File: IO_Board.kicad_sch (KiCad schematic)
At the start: 5 parts

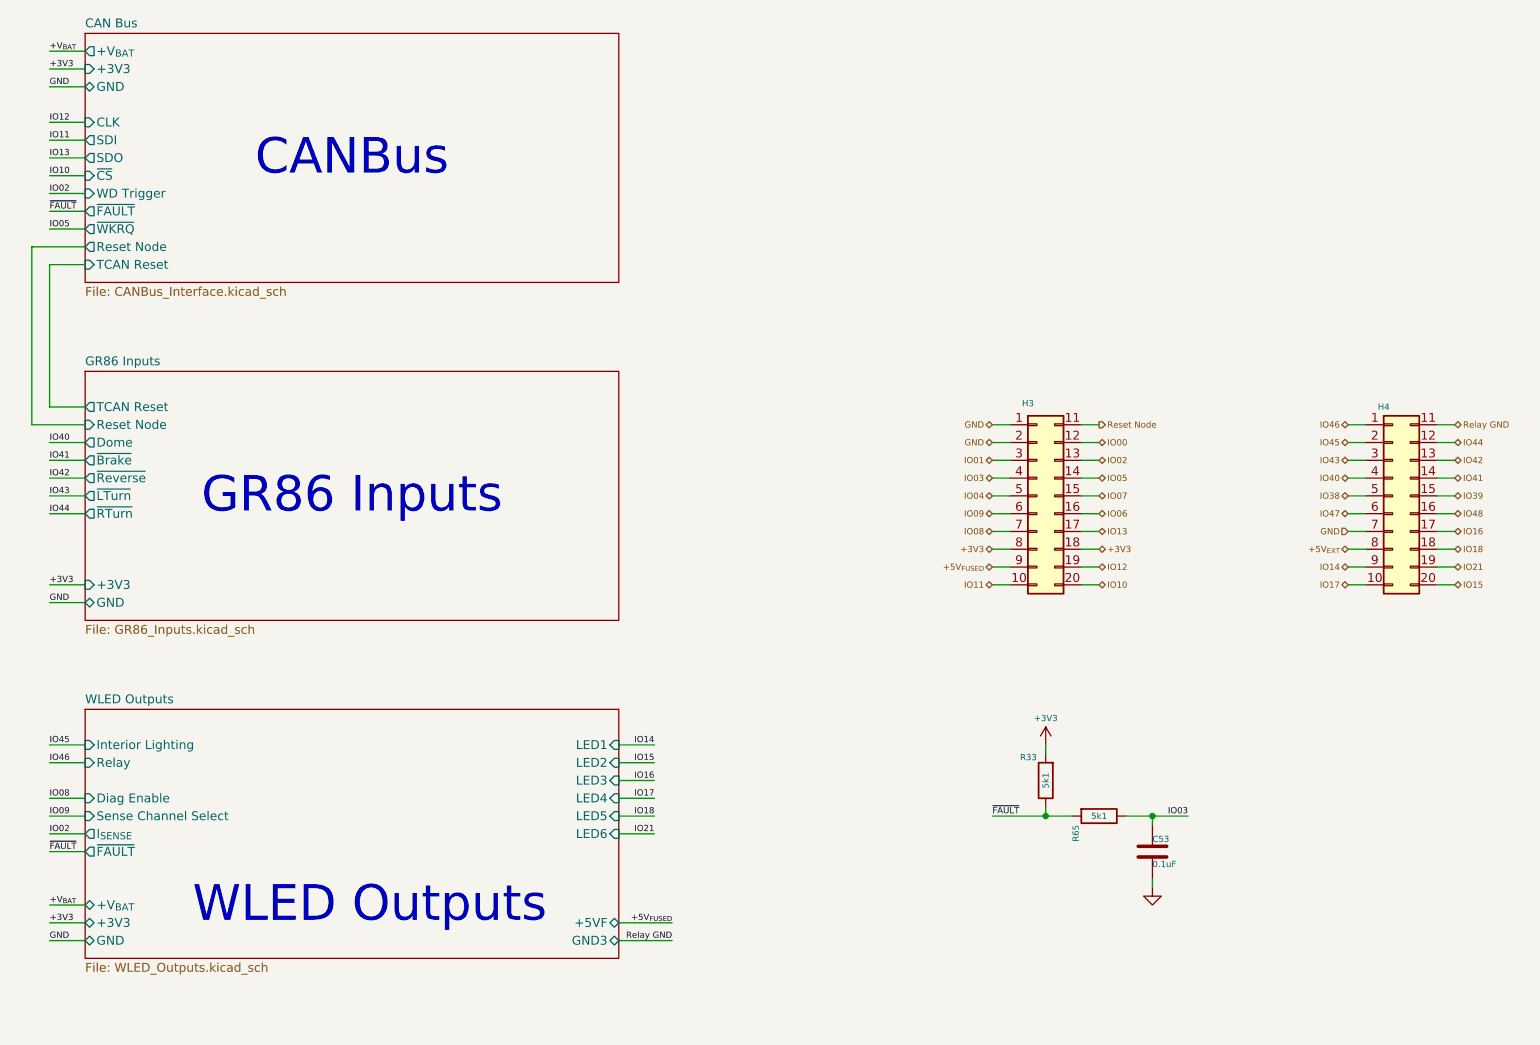
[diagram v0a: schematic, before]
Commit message: Update CANBus_Interface.kicad_sch, ESP32-S3 D1 Pico Board.kicad_sch, ESP32-S3 Pico D1.kicad_pcb, and 15 more files
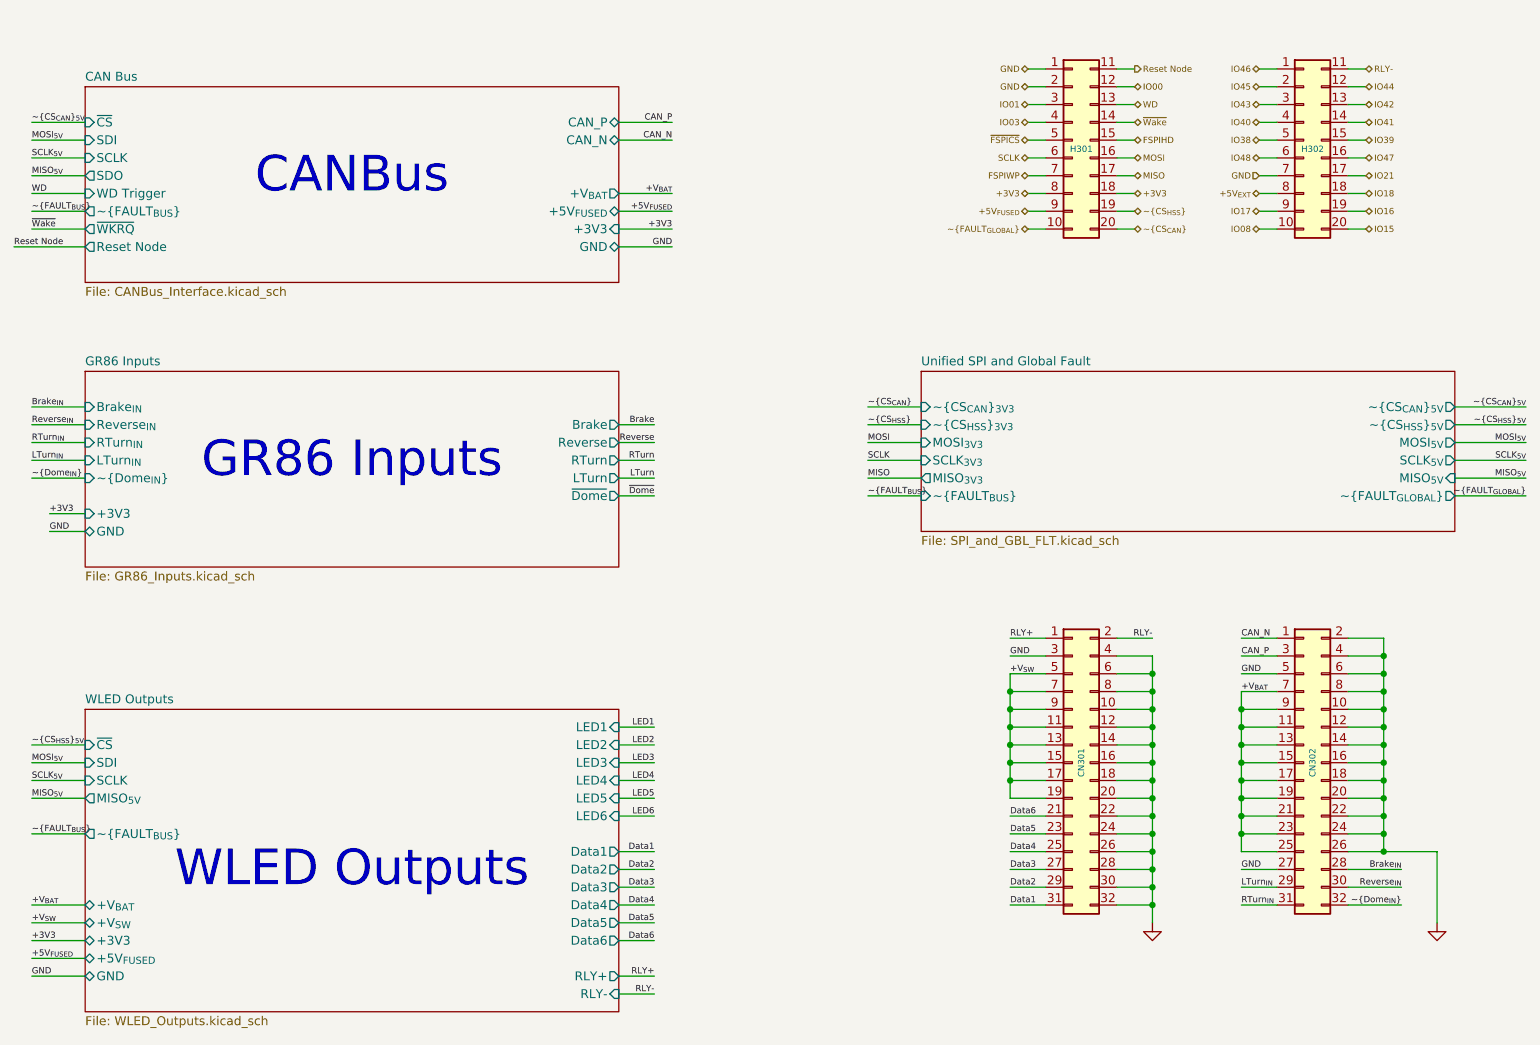
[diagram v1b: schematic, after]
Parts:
- removed C53: 0.1uF, Capacitors:C_0201_Dense, symbol Device:C
- removed R33, R65: 5k1, Resistors:R_0201_Dense, symbol Device:R
- added CN301, CN302: SM32B-NSHDZS-1-TF, My Connectors:JST_NSHD_SM32B-NSHD_2x16_P1.0mm_Horizontal_SMD, symbol PersonalSchematicSymbolLibrary:Conn_02x16_Odd_Even
- H301: renamed from H3; footprint Personal_FootprintLibrary:PinHeader_2x10_P2.54mm_LowProfile_BottomEntrySMD -> My Connectors:PinHeader_2x10_P2.54mm_Vertical_THT_BottomMount_TopReference
- H302: renamed from H4; footprint Personal_FootprintLibrary:PinHeader_2x10_P2.54mm_LowProfile_BottomEntrySMD -> My Connectors:PinHeader_2x10_P2.54mm_Vertical_THT_BottomMount_TopReference
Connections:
- net IO14 is gone; now on net IO17: H302.9 (Pin_9)
- net +V_{BAT}: now also CN302.11 (Pin_11), CN302.13 (Pin_13), CN302.15 (Pin_15), CN302.17 (Pin_17), CN302.19 (Pin_19), CN302.21 (Pin_21), CN302.23 (Pin_23), CN302.25 (Pin_23), CN302.7 (Pin_7), CN302.9 (Pin_9)
- net GND: now also CN301.10 (Pin_10), CN301.12 (Pin_12), CN301.14 (Pin_14), CN301.16 (Pin_16), CN301.18 (Pin_18), CN301.20 (Pin_20), CN301.22 (Pin_22), CN301.24 (Pin_24), CN301.26 (Pin_24), CN301.28 (Pin_24), CN301.3 (Pin_3), CN301.30 (Pin_24), CN301.32 (Pin_24), CN301.4 (Pin_4), CN301.6 (Pin_6), CN301.8 (Pin_8), CN302.10 (Pin_10), CN302.12 (Pin_12), CN302.14 (Pin_14), CN302.16 (Pin_16), CN302.18 (Pin_18), CN302.2 (Pin_2), CN302.20 (Pin_20), CN302.22 (Pin_22), CN302.24 (Pin_24), CN302.26 (Pin_24), CN302.27 (Pin_23), CN302.4 (Pin_4), CN302.5 (Pin_5), CN302.6 (Pin_6), CN302.8 (Pin_8)
- net IO08: now also H302.10 (Pin_10); no longer H301.7 (Pin_7)
- net IO16: now also H302.19 (Pin_19); no longer H302.17 (Pin_17)
- net IO17: no longer H302.10 (Pin_10)
- net IO21: now also H302.17 (Pin_17); no longer H302.19 (Pin_19)
- net IO47: now also H302.16 (Pin_16); no longer H302.6 (Pin_6)
- net IO48: now also H302.6 (Pin_6); no longer H302.16 (Pin_16)
- net IO02 renamed WD
- net IO04 renamed ~{FSPICS}
- net IO05 renamed ~{Wake}
- net IO06 renamed MOSI
- net IO07 renamed FSPIHD
- net IO09 renamed SCLK
- net IO10 renamed ~{CS_{CAN}}
- net IO11 renamed ~{FAULT_{GLOBAL}}
- net IO12 renamed ~{CS_{HSS}}
- net IO13 renamed MISO
- net Relay GND renamed RLY-
- net RLY-: now also CN301.2 (Pin_2)
- new net +V_{SW}: CN301.11 (Pin_11), CN301.13 (Pin_13), CN301.15 (Pin_15), CN301.17 (Pin_17), CN301.19 (Pin_19), CN301.5 (Pin_5), CN301.7 (Pin_7), CN301.9 (Pin_9)
- new net Brake_{IN}: CN302.28 (Pin_24)
- new net CAN_N: CN302.1 (Pin_1)
- new net CAN_P: CN302.3 (Pin_3)
- new net Data1: CN301.31 (Pin_23)
- new net Data2: CN301.29 (Pin_23)
- new net Data3: CN301.27 (Pin_23)
- new net Data4: CN301.25 (Pin_23)
- new net Data5: CN301.23 (Pin_23)
- new net Data6: CN301.21 (Pin_21)
- new net FSPIWP: H301.7 (Pin_7)
- new net LTurn_{IN}: CN302.29 (Pin_23)
- new net RLY+: CN301.1 (Pin_1)
- new net RTurn_{IN}: CN302.31 (Pin_23)
- new net Reverse_{IN}: CN302.30 (Pin_24)
- new net ~{Dome_{IN}}: CN302.32 (Pin_24)
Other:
- added sheet Unified SPI and Global Fault (SPI_and_GBL_FLT.kicad_sch)
- sheet CAN Bus ports: added +5V_{FUSED}, CAN_N, CAN_P, SCLK, ~{FAULT_{BUS}}; removed CLK, TCAN Reset, ~{FAULT}
- sheet GR86 Inputs ports: added Brake, Brake_{IN}, LTurn, LTurn_{IN}, RTurn, RTurn_{IN}, Reverse, Reverse_{IN}, ~{Dome_{IN}}, ~{Dome}; removed Dome, Reset Node, TCAN Reset, ~{Brake}, ~{LTurn}, ~{RTurn}, ~{Reverse}
- sheet WLED Outputs ports: added +5V_{FUSED}, +V_{SW}, Data1, Data2, Data3, Data4, Data5, Data6, MISO_{5V}, RLY+, RLY-, SCLK, SDI, ~{CS}, ~{FAULT_{BUS}}; removed +5VF, Diag Enable, GND3, I_{SENSE}, Interior Lighting, Relay, Sense Channel Select, ~{FAULT}
- moved on the sheet: H301, H302
